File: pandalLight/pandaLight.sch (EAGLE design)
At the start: 120 parts, among them J1 PJ-037A, U13 TPD12S016PWR, U15 PMOD-2X6, U16 PMOD-2X6, U17 PLR135-T10, U18 PLT133-T10W, U20 TP10SQ, U21 TP10SQ, U22 PAN1322, U23 6SLX9TQG144, U3 TPD4S014SON, U4 FT2232HL, U5 93LC46BT-I/OT, U6 51, U7 51, U8 TPD12S016PWR, X1 USBUB-S, X2 HDMI_RECEPTICAL_A, X4 HDMI_RECEPTICAL_A, Y1 403, Y2 20Mhz

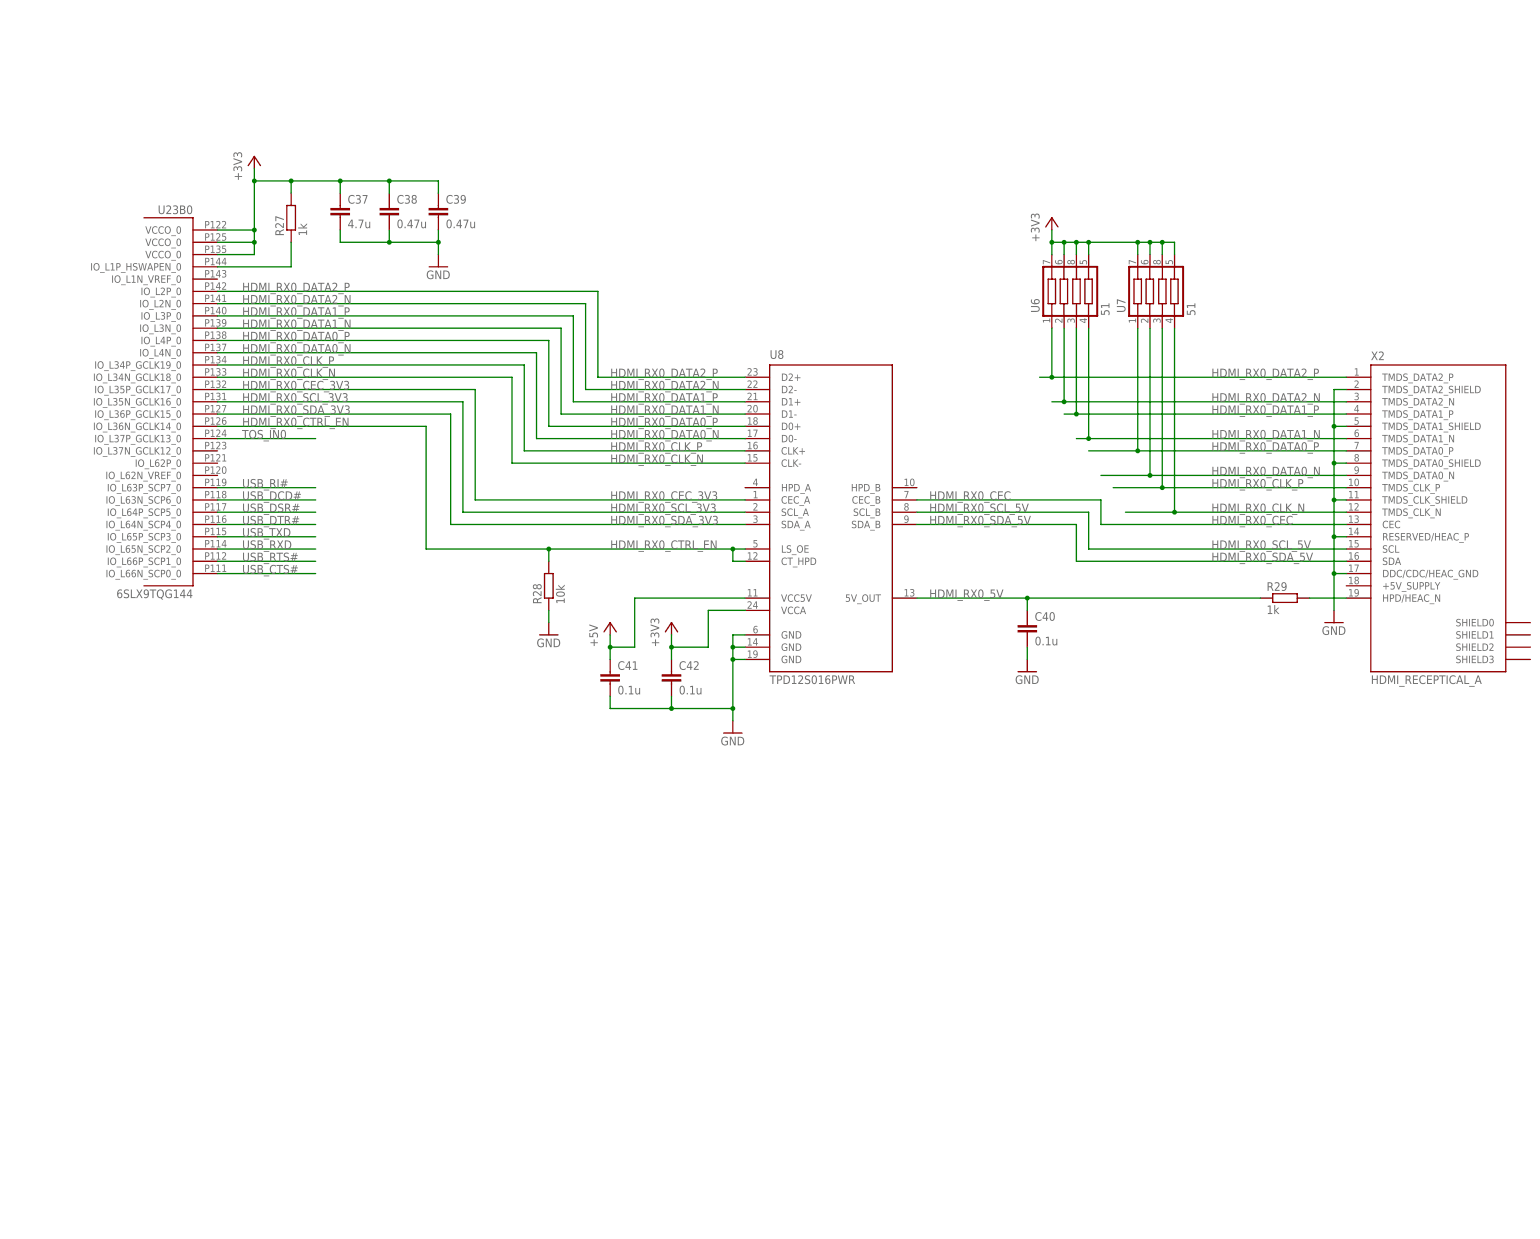
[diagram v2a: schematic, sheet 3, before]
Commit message: Created BOM; Began routing; Changed to available LEDs
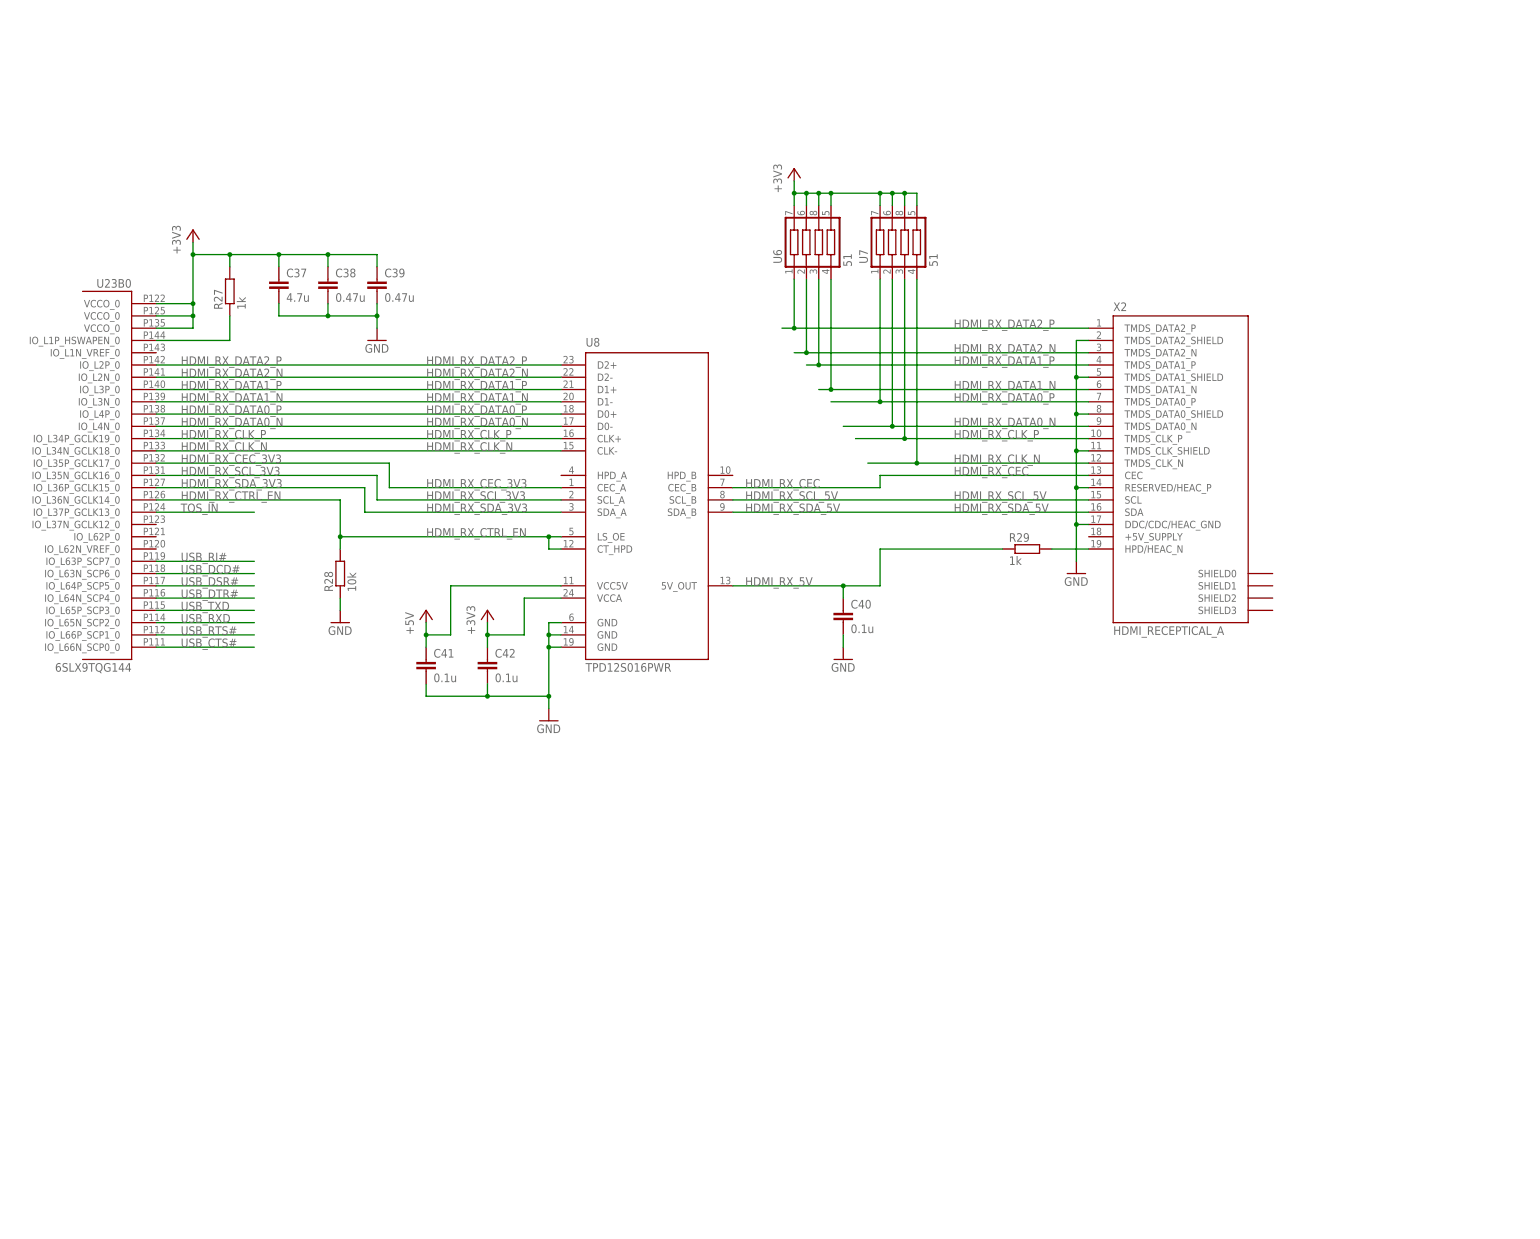
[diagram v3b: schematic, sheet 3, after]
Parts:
- removed C1: 100u, pandaLight:CAPACITOR1206
- removed LED3: Green, pandaLight:LED0603
- removed LED4: Yellow, pandaLight:LED0603
- removed R30, R31: 1k, pandaLight:RESISTOR0402
- C13, C14: PARTNO (none) -> CL10A106MQ8NNNC
- LED1: PARTNO LG Q971-KN-1 -> LTST-C191KGKT
- LED2: PARTNO LY Q976-P1S2-36 -> LTST-C191KSKT
- SV3: value (none) -> LEDS_CON; device pandaLight:MA02-1 -> pandaLight:MA04-1; BOM (none) -> EXCLUDE; PARTNO (none) -> *
- U$1: PARTNO (none) -> M25P40-VMN6PB
- U$2: PARTNO (none) -> MIC2230-S4YML TR
- U23: PARTNO (none) -> XC6SLX9-3TQG144C
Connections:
- net HDMI_RX0_5V renamed HDMI_RX_5V
- net HDMI_RX0_CEC renamed HDMI_RX_CEC
- net HDMI_RX0_CEC_3V3 renamed HDMI_RX_CEC_3V3
- net HDMI_RX0_CLK_N renamed HDMI_RX_CLK_N
- net HDMI_RX0_CLK_P renamed HDMI_RX_CLK_P
- net HDMI_RX0_CTRL_EN renamed HDMI_RX_CTRL_EN
- net HDMI_RX0_DATA0_N renamed HDMI_RX_DATA0_N
- net HDMI_RX0_DATA0_P renamed HDMI_RX_DATA0_P
- net HDMI_RX0_DATA1_N renamed HDMI_RX_DATA1_N
- net HDMI_RX0_DATA1_P renamed HDMI_RX_DATA1_P
- net HDMI_RX0_DATA2_N renamed HDMI_RX_DATA2_N
- net HDMI_RX0_DATA2_P renamed HDMI_RX_DATA2_P
- net HDMI_RX0_SCL_3V3 renamed HDMI_RX_SCL_3V3
- net HDMI_RX0_SCL_5V renamed HDMI_RX_SCL_5V
- net HDMI_RX0_SDA_3V3 renamed HDMI_RX_SDA_3V3
- net HDMI_RX0_SDA_5V renamed HDMI_RX_SDA_5V
- net HDMI_TX0_5V renamed HDMI_TX_5V
- net HDMI_TX0_CEC renamed HDMI_TX_CEC
- net HDMI_TX0_CEC_3V3 renamed HDMI_TX_CEC_3V3
- net HDMI_TX0_CLK_N renamed HDMI_TX_CLK_N
- net HDMI_TX0_CLK_P renamed HDMI_TX_CLK_P
- net HDMI_TX0_CTRL_EN renamed HDMI_TX_CTRL_EN
- net HDMI_TX0_DATA0_N renamed HDMI_TX_DATA0_N
- net HDMI_TX0_DATA0_P renamed HDMI_TX_DATA0_P
- net HDMI_TX0_DATA1_N renamed HDMI_TX_DATA1_N
- net HDMI_TX0_DATA1_P renamed HDMI_TX_DATA1_P
- net HDMI_TX0_DATA2_N renamed HDMI_TX_DATA2_N
- net HDMI_TX0_HPD_5V renamed HDMI_TX_HPD_5V
- net HDMI_TX0_SCL_3V3 renamed HDMI_TX_SCL_3V3
- net HDMI_TX0_SCL_5V renamed HDMI_TX_SCL_5V
- net HDMI_TX0_SDA_3V3 renamed HDMI_TX_SDA_3V3
- net HDMI_TX0_SDA_5V renamed HDMI_TX_SDA_5V
- net TOS_IN0 renamed TOS_IN
- net TOS_OUT0 renamed TOS_OUT
- removed net CENTER: C6.1, J1.CENTER, JP1.1, SV1.1
- removed net HDMI_TX0_DATA2_P: X4.TMDS_DATA2_P
- removed net N$3: LED4.A, R31.1
- removed net N$37: LED3.A, R30.1
- removed net N$44: U13.D2+, U23B2.IO_L12P_D1_MISO2_2
- removed net USB_RXLED#: LED3.C, U4.BCBUS3
- removed net USB_TXLED#: LED4.C, U4.BCBUS4
- new net 5V_SUP: C6.1, J1.CENTER, JP1.1, SV1.1, SV3.1
- new net HDMI_TX_DATA2_P: U13.D2+, U23B2.IO_L12P_D1_MISO2_2, X4.TMDS_DATA2_P
- net +3V3: no longer R30.2, R31.2
- net +5V: no longer C1.1
- net GND: now also SV3.4, U$2.EP; no longer C1.2
- net LEDS_CLK: now also SV3.3; no longer SV3.2
- net LEDS_DATA: now also SV3.2; no longer SV3.1
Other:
- moved on the sheet: C37, C38, C39, C40, C41, C42, C43, C53, C54, C55, C56, C57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

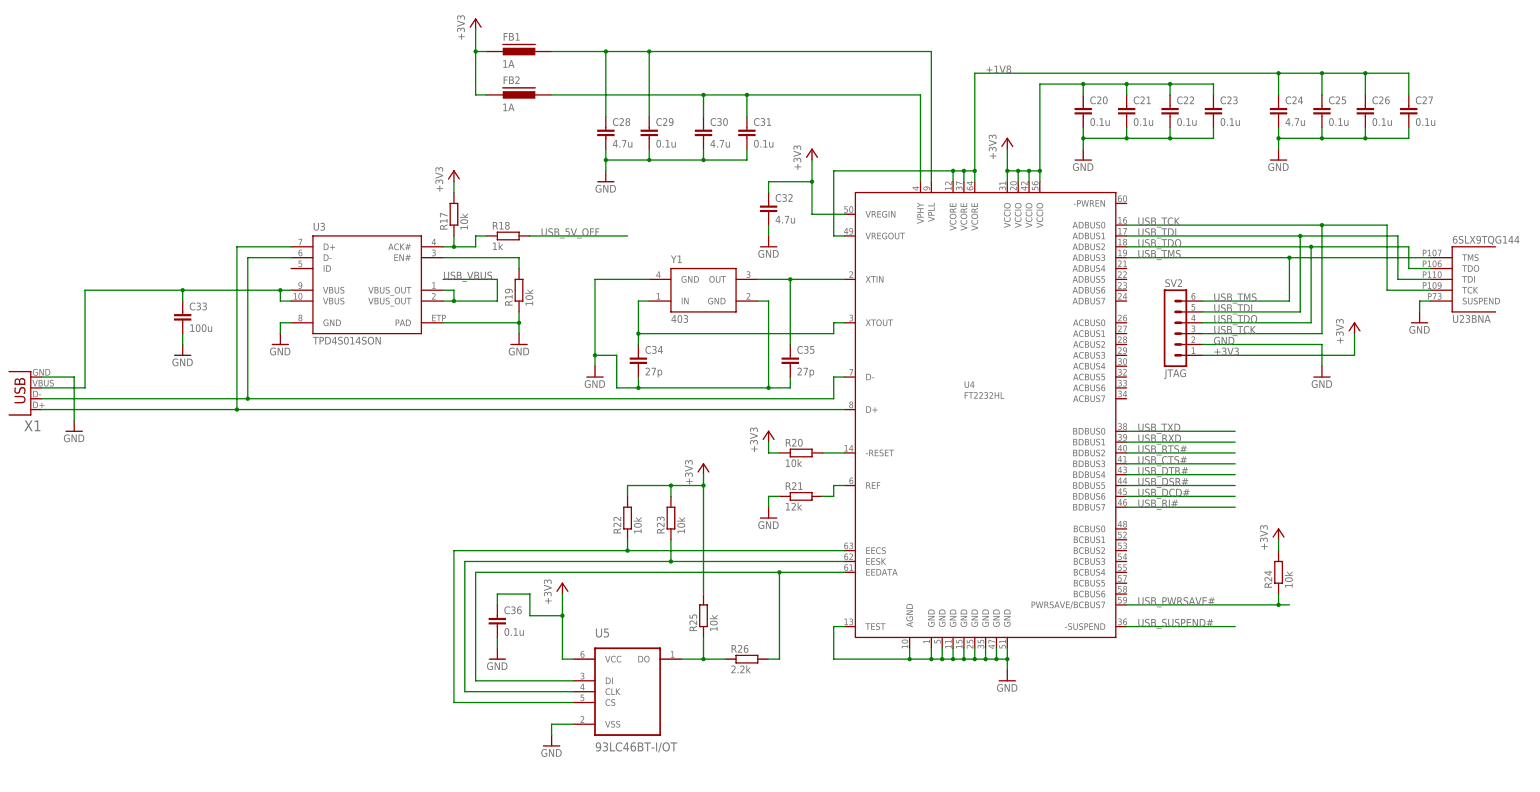
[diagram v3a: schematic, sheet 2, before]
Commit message: Removed the USB companion chip; Routed USB part
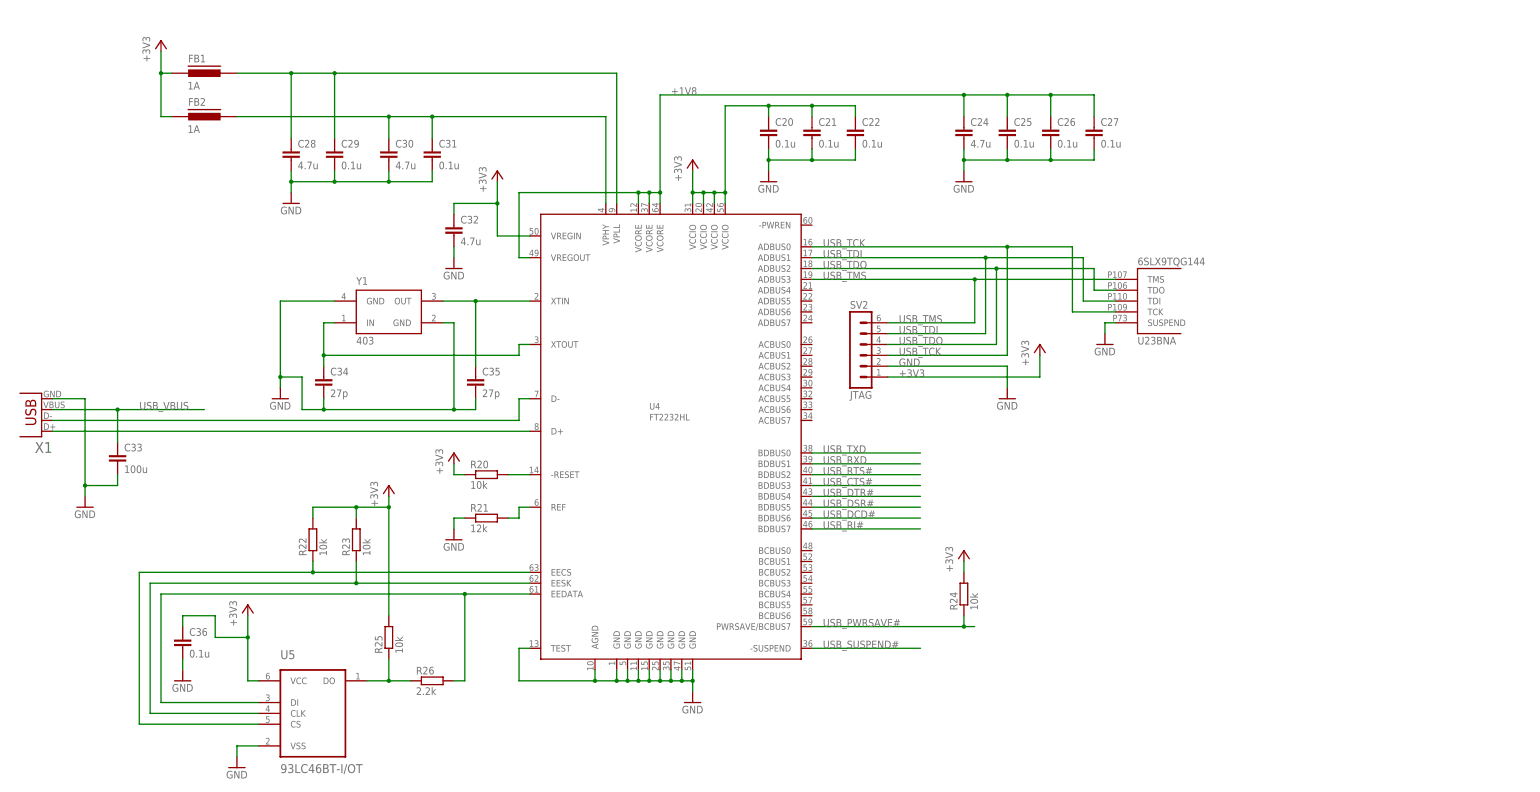
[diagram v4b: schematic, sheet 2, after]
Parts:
- removed C23: 0.1u, pandaLight:CAPACITOR0402
- removed R17, R19: 10k, pandaLight:RESISTOR0402
- removed R18: 1k, pandaLight:RESISTOR0402
- removed U3: TPD4S014SON, pandaLight:TPD4S014SON
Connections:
- removed net N$45: C33.1, U3.VBUS@10, U3.VBUS@9, X1.VBUS
- removed net USB_5V_ACK#: R17.1, R18.1, U3.ACK#
- removed net USB_5V_DISABLE: R19.2, U3.EN#
- removed net USB_5V_OFF: R18.2
- net +3V3: no longer C23.1, R17.2
- net GND: no longer C23.2, R19.1, U3.GND, U3.PAD
- net N$7: no longer U3.D-
- net N$8: no longer U3.D+
- net USB_VBUS: now also C33.1, X1.VBUS; no longer U3.VBUS_OUT@1, U3.VBUS_OUT@2
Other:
- moved on the sheet: C20, C21, C22, C24, C25, C26, C27, C28, C29, C30, C31, C32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

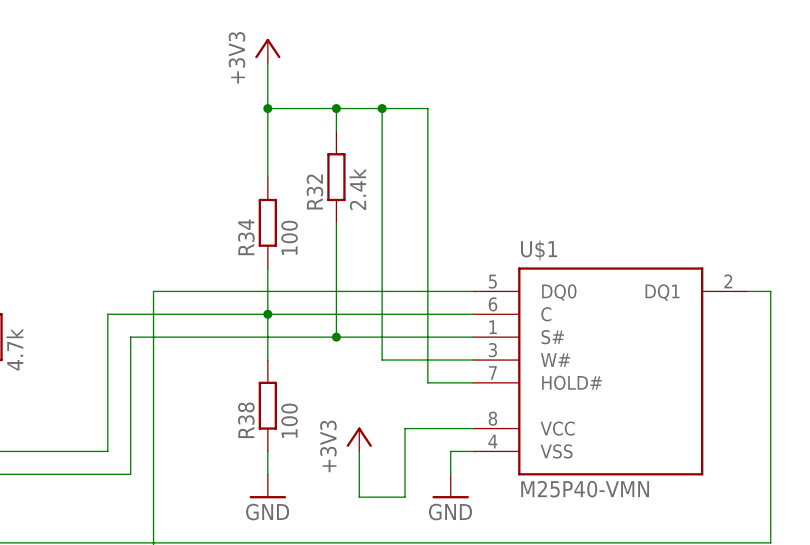
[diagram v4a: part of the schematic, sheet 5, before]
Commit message: Routed HDMI TX
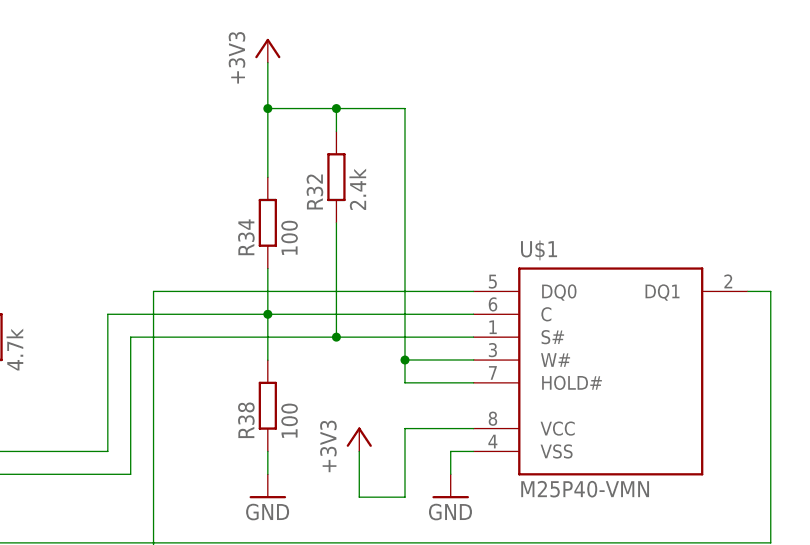
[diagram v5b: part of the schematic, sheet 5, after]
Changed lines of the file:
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@@
 <pinref part="R32" gate="G$1" pin="2"/>
 <wire x1="147.32" y1="139.7" x2="147.32" y2="142.24" width="0.1524" layer="91"/>
-<wire x1="147.32" y1="142.24" x2="152.4" y2="142.24" width="0.1524" layer="91"/>
 <junction x="147.32" y="142.24"/>
-<wire x1="152.4" y1="142.24" x2="157.48" y2="142.24" width="0.1524" layer="91"/>
-<junction x="152.4" y="142.24"/>
+<wire x1="147.32" y1="142.24" x2="154.94" y2="142.24" width="0.1524" layer="91"/>
 <pinref part="R34" gate="G$1" pin="2"/>
 <wire x1="139.7" y1="134.62" x2="139.7" y2="142.24" width="0.1524" layer="91"/>
@@
 <wire x1="139.7" y1="142.24" x2="139.7" y2="147.32" width="0.1524" layer="91"/>
 <junction x="139.7" y="142.24"/>
-<wire x1="162.56" y1="114.3" x2="152.4" y2="114.3" width="0.1524" layer="91"/>
-<wire x1="152.4" y1="142.24" x2="152.4" y2="114.3" width="0.1524" layer="91"/>
-<wire x1="157.48" y1="111.76" x2="162.56" y2="111.76" width="0.1524" layer="91"/>
-<wire x1="157.48" y1="111.76" x2="157.48" y2="142.24" width="0.1524" layer="91"/>
+<wire x1="154.94" y1="111.76" x2="162.56" y2="111.76" width="0.1524" layer="91"/>
+<wire x1="154.94" y1="111.76" x2="154.94" y2="114.3" width="0.1524" layer="91"/>
+<pinref part="U$1" gate="G$1" pin="HOLD#"/>
 <pinref part="U$1" gate="G$1" pin="W#"/>
-<pinref part="U$1" gate="G$1" pin="HOLD#"/>
+<wire x1="154.94" y1="114.3" x2="154.94" y2="142.24" width="0.1524" layer="91"/>
+<wire x1="162.56" y1="114.3" x2="154.94" y2="114.3" width="0.1524" layer="91"/>
+<junction x="154.94" y="114.3"/>
 </segment>
 <segment>
@@
 </segment>
 </net>
-<net name="HDMI_TX_DATA2_P" class="0">
+<net name="HDMI_TX_DATA2_P" class="2">
 <segment>
 <pinref part="U13" gate="G$1" pin="D2+"/>
